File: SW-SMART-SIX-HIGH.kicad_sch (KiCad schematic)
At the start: 99 parts, among them J1 SWD, J2 USART2, J3 POWER OUT, J4 POWER IN, J5 POWER OUT, SW0 BTS7002-1EPP, SW1 BTS7002-1EPP, SW2 BTS7002-1EPP, SW3 BTS7002-1EPP, SW4 BTS7002-1EPP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

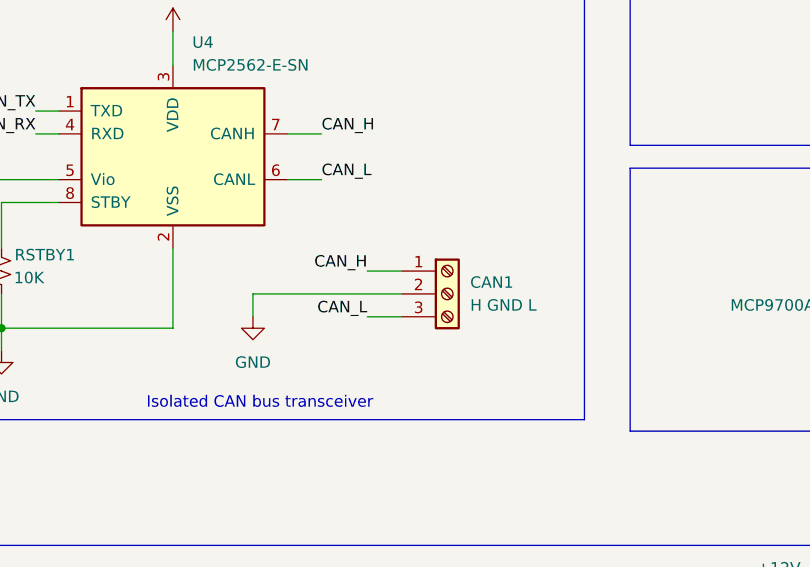
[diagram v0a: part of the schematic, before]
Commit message: updated can bus connector footprint
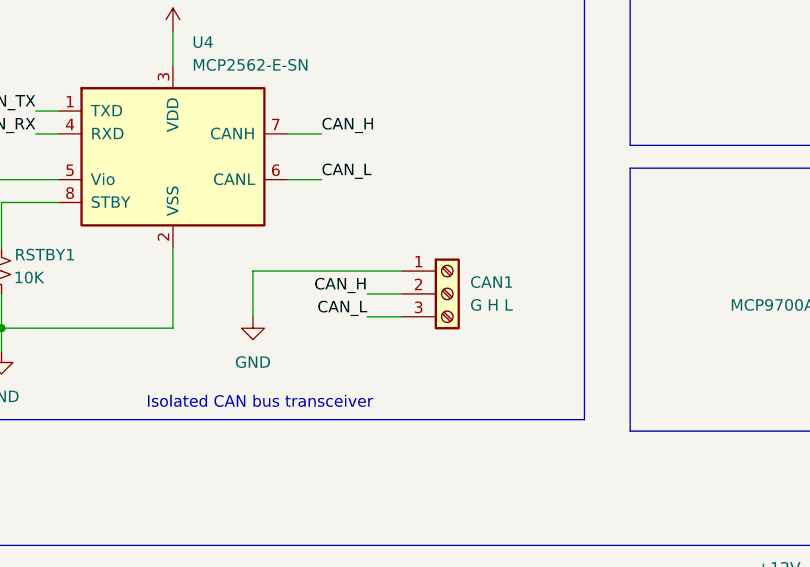
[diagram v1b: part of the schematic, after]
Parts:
- CAN1: value H GND L -> G H L; footprint TerminalBlock_Phoenix:TerminalBlock_Phoenix_MKDS-1,5-3-5.08_1x03_P5.08mm_Horizontal -> TerminalBlock_Phoenix:TerminalBlock_Phoenix_MPT-0,5-3-2.54_1x03_P2.54mm_Horizontal
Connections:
- net CAN_H: now also CAN1.2 (Pin_2); no longer CAN1.1 (Pin_1)
- net GND: now also CAN1.1 (Pin_1); no longer CAN1.2 (Pin_2)
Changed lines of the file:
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@@
 	(wire
 		(pts
-			(xy 147.32 83.82) (xy 147.32 86.36)
+			(xy 147.32 81.28) (xy 147.32 86.36)
 		)
 		(stroke
@@
 	(wire
 		(pts
+			(xy 160.02 83.82) (xy 163.83 83.82)
+		)
+		(stroke
+			(width 0)
+			(type default)
+		)
+	)
+	(wire
+		(pts
 			(xy 353.06 199.39) (xy 359.41 199.39)
 		)
@@
 	(wire
 		(pts
-			(xy 160.02 81.28) (xy 163.83 81.28)
-		)
-		(stroke
-			(width 0)
-			(type default)
-		)
-	)
-	(wire
-		(pts
 			(xy 306.07 96.52) (xy 316.23 96.52)
 		)
@@
 	(wire
 		(pts
+			(xy 147.32 81.28) (xy 163.83 81.28)
+		)
+		(stroke
+			(width 0)
+			(type default)
+		)
+	)
+	(wire
+		(pts
 			(xy 177.8 172.72) (xy 181.61 172.72)
 		)
@@
 	(wire
 		(pts
-			(xy 147.32 83.82) (xy 163.83 83.82)
-		)
-		(stroke
-			(width 0)
-			(type default)
-		)
-	)
-	(wire
-		(pts
 			(xy 92.71 49.53) (xy 92.71 60.96)
 		)
@@
 	)
 	(label "CAN_H"
-		(at 160.02 81.28 180)
+		(at 160.02 83.82 180)
 		(effects
 			(font
@@
 			)
 		)
-		(property "Value" "H GND L"
+		(property "Value" "G H L"
 			(at 171.45 85.0899 0)
 			(effects
@@
 			)
 		)
-		(property "Footprint" "TerminalBlock_Phoenix:TerminalBlock_Phoenix_MKDS-1,5-3-5.08_1x03_P5.08mm_Horizontal"
+		(property "Footprint" "TerminalBlock_Phoenix:TerminalBlock_Phoenix_MPT-0,5-3-2.54_1x03_P2.54mm_Horizontal"
 			(at 168.91 83.82 0)
 			(effects

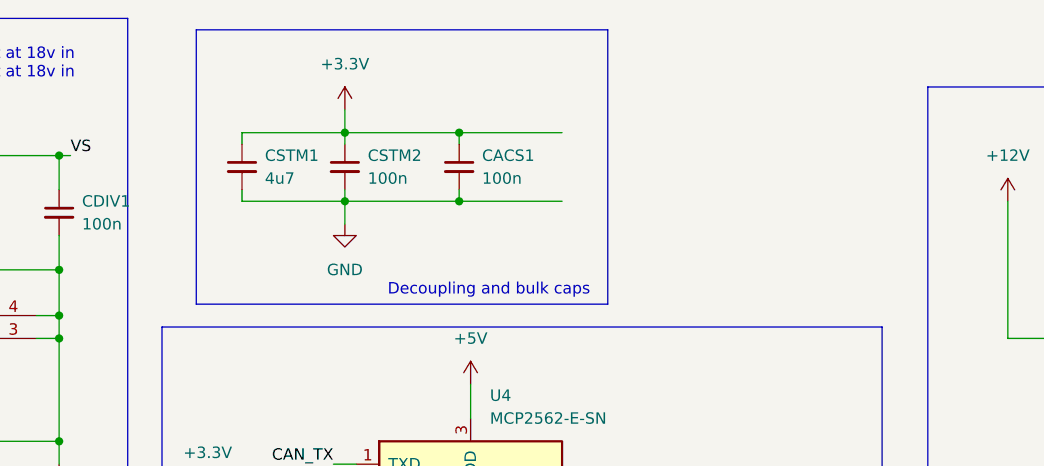
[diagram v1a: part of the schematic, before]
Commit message: added recommended mcu vref capacitors
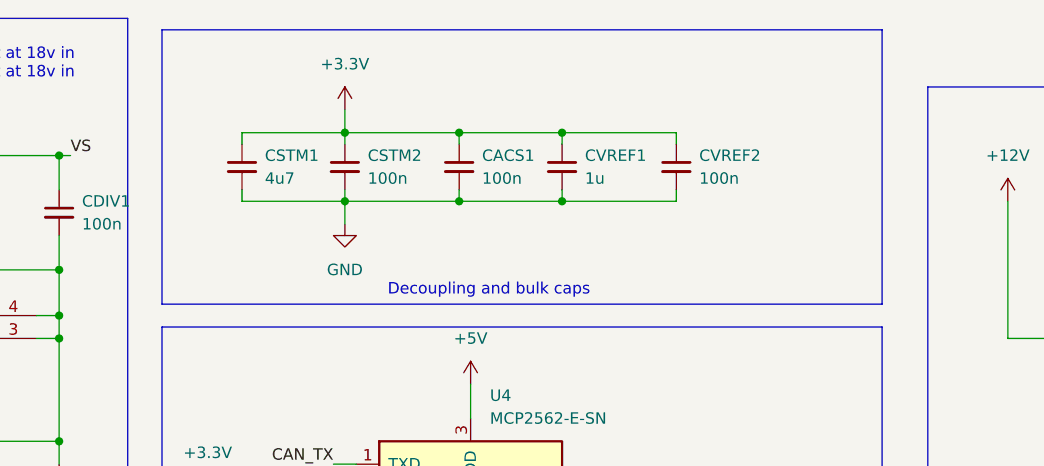
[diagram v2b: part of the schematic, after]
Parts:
- added CVREF1: 1u, Capacitor_SMD:C_0805_2012Metric_Pad1.18x1.45mm_HandSolder, symbol Device:C_Small
- added CVREF2: 100n, Capacitor_SMD:C_0603_1608Metric_Pad1.08x0.95mm_HandSolder, symbol Device:C_Small
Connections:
- net +3.3V: now also CVREF1.1, CVREF2.1
- net GND: now also CVREF1.2, CVREF2.2
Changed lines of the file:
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@@
 	)
 	(rectangle
-		(start 107.95 15.24)
-		(end 153.67 45.72)
+		(start 104.14 15.24)
+		(end 184.15 45.72)
 		(stroke
 			(width 0)
@@
 	)
 	(junction
+		(at 148.59 34.29)
+		(diameter 0)
+		(color 0 0 0 0)
+	)
+	(junction
 		(at 222.25 227.33)
 		(diameter 0)
@@
 	)
 	(junction
+		(at 148.59 26.67)
+		(diameter 0)
+		(color 0 0 0 0)
+	)
+	(junction
 		(at 68.58 29.21)
 		(diameter 0)
@@
 	(wire
 		(pts
+			(xy 161.29 26.67) (xy 161.29 27.94)
+		)
+		(stroke
+			(width 0)
+			(type default)
+		)
+	)
+	(wire
+		(pts
 			(xy 233.68 83.82) (xy 237.49 83.82)
 		)
@@
 	(wire
 		(pts
+			(xy 161.29 34.29) (xy 161.29 33.02)
+		)
+		(stroke
+			(width 0)
+			(type default)
+		)
+	)
+	(wire
+		(pts
 			(xy 222.25 177.8) (xy 222.25 181.61)
 		)
@@
 	(wire
 		(pts
+			(xy 148.59 26.67) (xy 148.59 27.94)
+		)
+		(stroke
+			(width 0)
+			(type default)
+		)
+	)
+	(wire
+		(pts
+			(xy 148.59 33.02) (xy 148.59 34.29)
+		)
+		(stroke
+			(width 0)
+			(type default)
+		)
+	)
+	(wire
+		(pts
 			(xy 177.8 177.8) (xy 181.61 177.8)
 		)
@@
 	(wire
 		(pts
+			(xy 148.59 26.67) (xy 161.29 26.67)
+		)
+		(stroke
+			(width 0)
+			(type default)
+		)
+	)
+	(wire
+		(pts
 			(xy 177.8 232.41) (xy 181.61 232.41)
 		)
@@
 	(wire
 		(pts
+			(xy 148.59 34.29) (xy 161.29 34.29)
+		)
+		(stroke
+			(width 0)
+			(type default)
+		)
+	)
+	(wire
+		(pts
 			(xy 238.76 189.23) (xy 238.76 191.77)
 		)
@@
 	)
 	(symbol
+		(lib_id "Device:C_Small")
+		(at 161.29 30.48 0)
+		(unit 1)
+		(exclude_from_sim no)
+		(in_bom yes)
+		(on_board yes)
+		(dnp no)
+		(fields_autoplaced yes)
+		(property "Reference" "CVREF2"
+			(at 163.83 29.2162 0)
+			(effects
+				(font
+					(size 1.27 1.27)
+				)
+				(justify left)
+			)
+		)
+		(property "Value" "100n"
+			(at 163.83 31.7562 0)
+			(effects
+				(font
+					(size 1.27 1.27)
+				)
+				(justify left)
+			)
+		)
+		(property "Footprint" "Capacitor_SMD:C_0603_1608Metric_Pad1.08x0.95mm_HandSolder"
+			(at 161.29 30.48 0)
+			(effects
+				(font
+					(size 1.27 1.27)
+				)
+				(hide yes)
+			)
+		)
+		(property "Datasheet" "~"
+			(at 161.29 30.48 0)
+			(effects
+				(font
+					(size 1.27 1.27)
+				)
+				(hide yes)
+			)
+		)
+		(property "Description" "Unpolarized capacitor, small symbol"
+			(at 161.29 30.48 0)
+			(effects
+				(font
+					(size 1.27 1.27)
+				)
+				(hide yes)
+			)
+		)
+		(pin "2"
+		)
+		(pin "1"
+		)
+		(instances
+			(project "SW-SMART-SIX-HIGH"
+				(path "/08d9f551-d314-4c5c-859f-da02a807087d"
+					(reference "CVREF2")
+					(unit 1)
+				)
+			)
+		)
+	)
+	(symbol
 		(lib_id "power:GND")
 		(at 107.95 189.23 0)
@@
 					(unit 1)
 				)
+			)
+		)
+	)
+	(symbol
+		(lib_id "Device:C_Small")
+		(at 148.59 30.48 0)
+		(unit 1)
+		(exclude_from_sim no)
+		(in_bom yes)
+		(on_board yes)
+		(dnp no)
+		(fields_autoplaced yes)
+		(property "Reference" "CVREF1"
+			(at 151.13 29.2162 0)
+			(effects
+				(font
+					(size 1.27 1.27)
+				)
+				(justify left)
+			)
+		)
+		(property "Value" "1u"
+			(at 151.13 31.7562 0)
+			(effects
+				(font
+					(size 1.27 1.27)
+				)
+				(justify left)
+			)
+		)
+		(property "Footprint" "Capacitor_SMD:C_0805_2012Metric_Pad1.18x1.45mm_HandSolder"
+			(at 148.59 30.48 0)
+			(effects
+				(font
+					(size 1.27 1.27)
+				)
+				(hide yes)
+			)
+		)
+		(property "Datasheet" "~"
+			(at 148.59 30.48 0)
+			(effects
+				(font
+					(size 1.27 1.27)
+				)
+				(hide yes)
+			)
+		)
+		(property "Description" "Unpolarized capacitor, small symbol"
+			(at 148.59 30.48 0)
+			(effects
+				(font
+					(size 1.27 1.27)
+				)
+				(hide yes)
+			)
+		)
+		(pin "2"
+		)
+		(pin "1"
+		)
+		(instances
+			(project "SW-SMART-SIX-HIGH"
+				(path "/08d9f551-d314-4c5c-859f-da02a807087d"
+					(reference "CVREF1")
+					(unit 1)
+				)

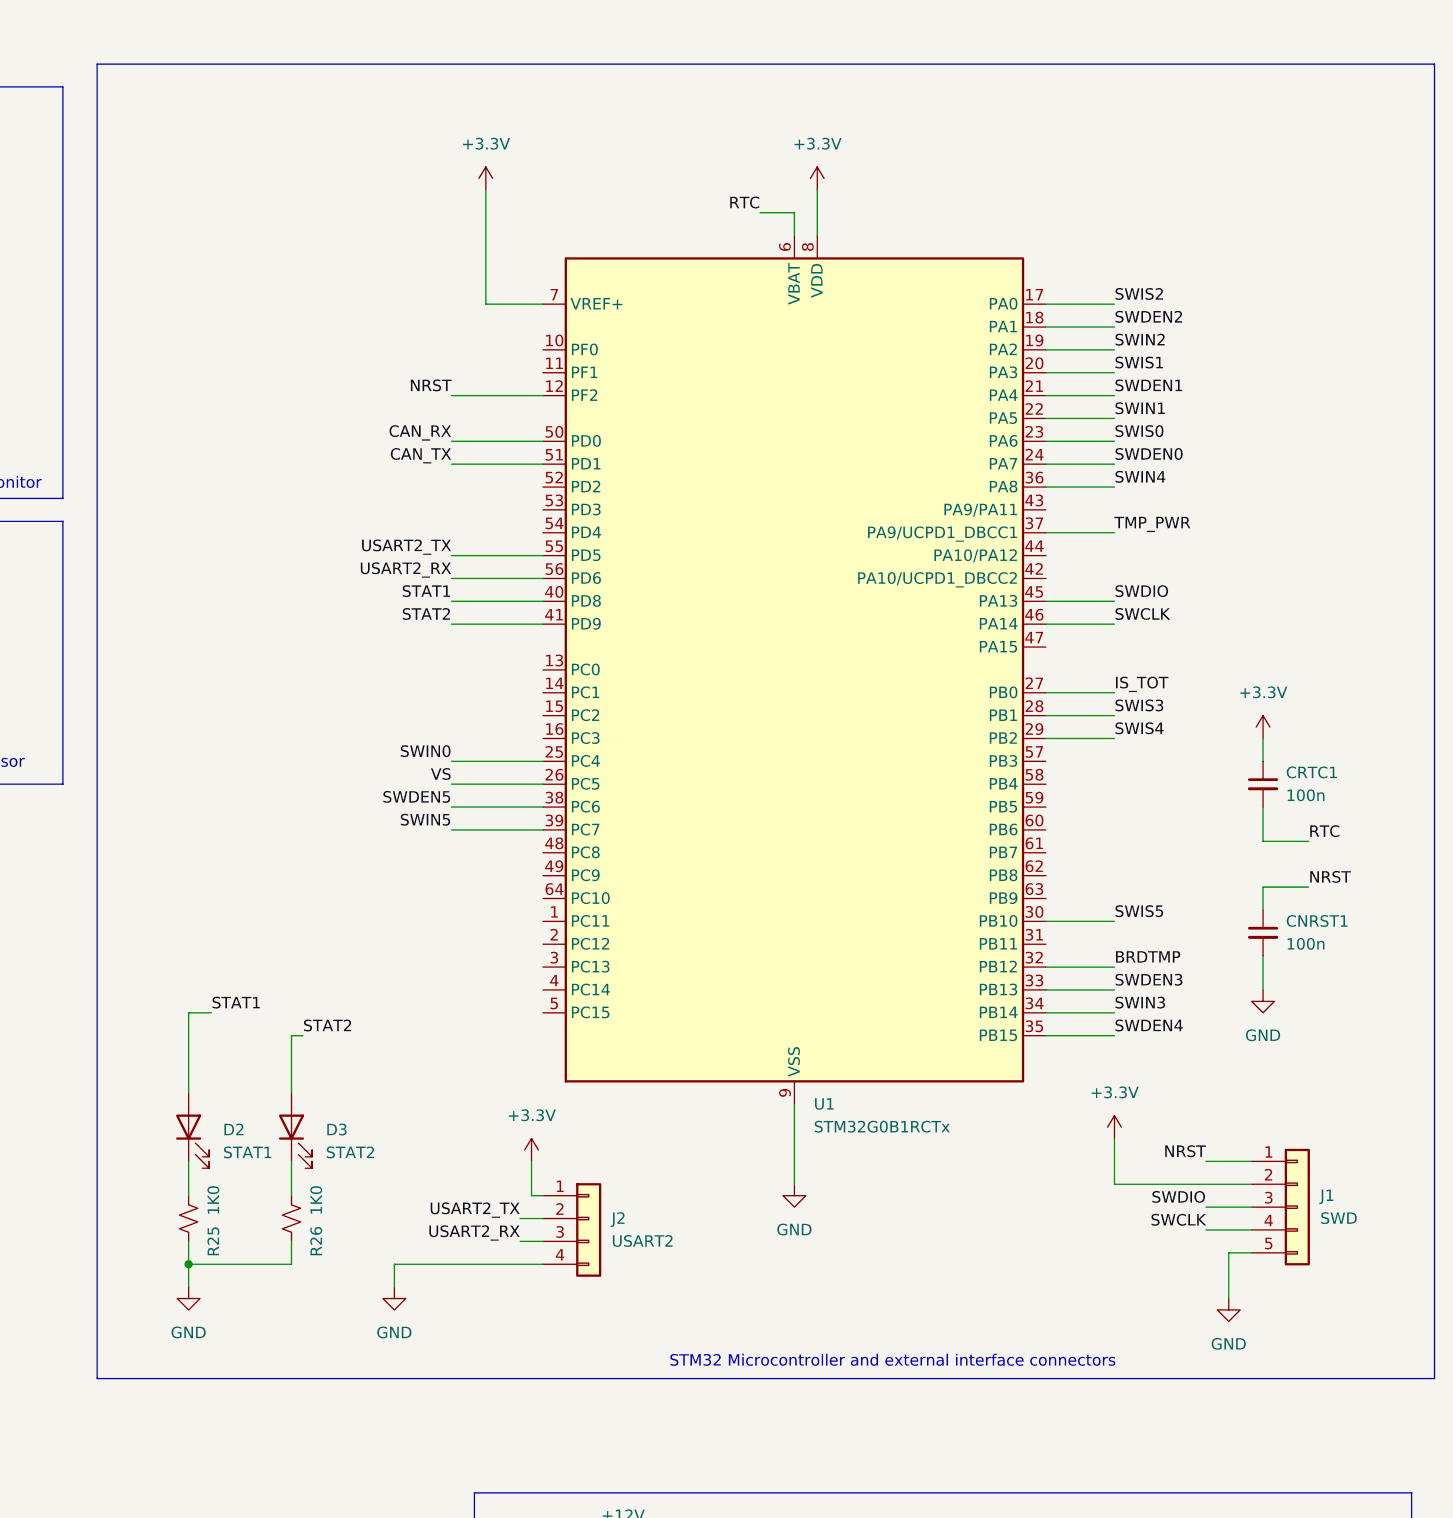
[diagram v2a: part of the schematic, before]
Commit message: added crystal osc
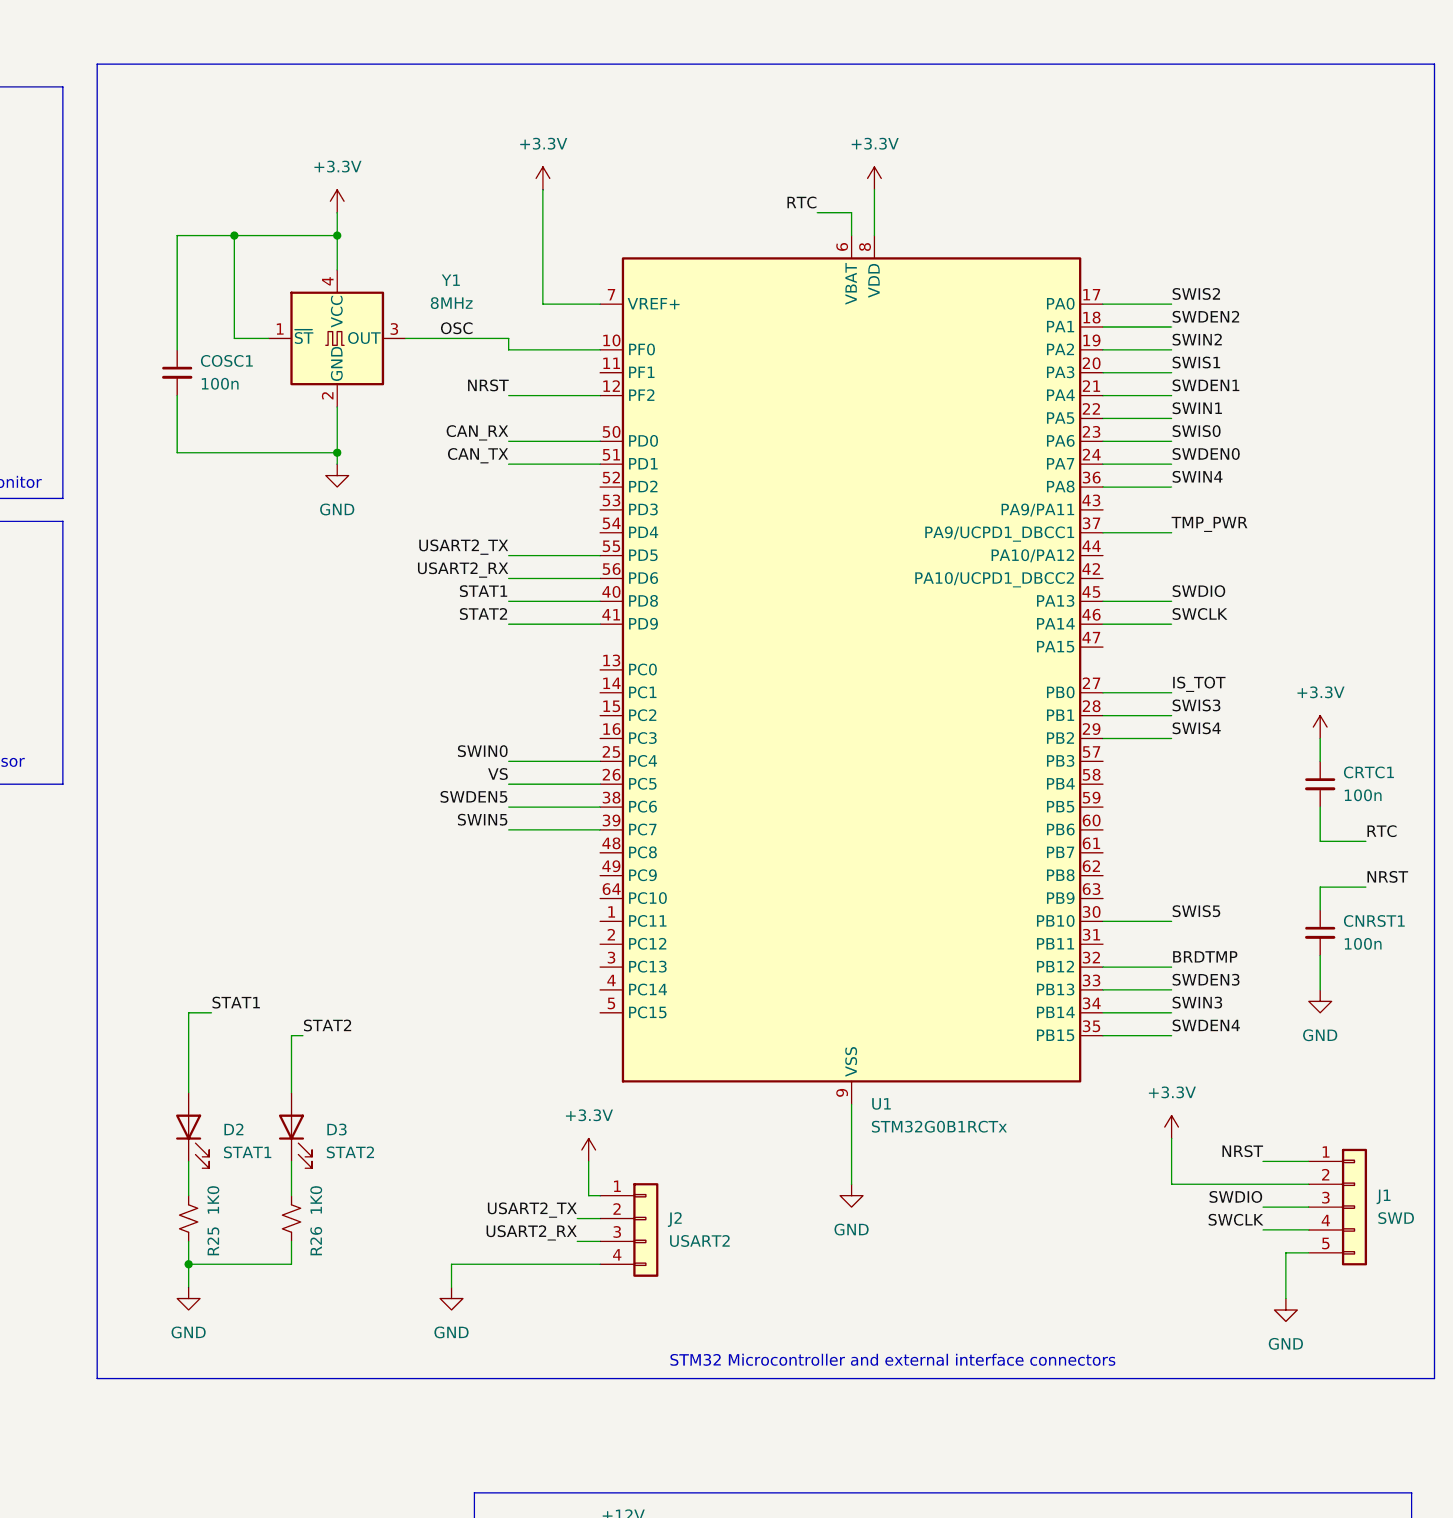
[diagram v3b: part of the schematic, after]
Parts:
- added COSC1: 100n, Capacitor_SMD:C_0603_1608Metric_Pad1.08x0.95mm_HandSolder, symbol Device:C_Small
- added Y1: 8MHz, Oscillator:Oscillator_SMD_EuroQuartz_XO32-4Pin_3.2x2.5mm_RotB_HandSoldering, symbol Oscillator:SG-5032CAN
- L1: footprint SRP5030HMT-8R2M -> SamacSys_Parts:SRP5030HMT2R2M
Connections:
- net +3.3V: now also COSC1.1, Y1.1 (~{ST}), Y1.4 (VCC)
- net GND: now also COSC1.2, Y1.2 (GND)
- net OSC: now reaches U1.10 (PF0)
- net OSC: now also Y1.3 (OUT)
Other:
- moved on the sheet: CNRST1, CRTC1, J1, J2, U1
